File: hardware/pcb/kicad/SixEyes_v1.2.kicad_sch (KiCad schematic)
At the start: 49 parts, among them M1 NEMA17 40mm, U1 AS5600 Module

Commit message: Update the joint board for UART mode and the new pin map
MS1 and MS2 move to GPIO15 and GPIO16, UART TX to GPIO5, and the module's VREF
pad is read on GPIO2 through a new 10k resistor (R5). Adds the JDR4 socket for
the module's VREF and DIAG pads, VM and EN markers, a corrected regulator label,
JLCPCB 4-layer stackup and limits, net classes, and custom design rules for
power track widths, via sizes and the CAN pair. BOM gains the second 10k
resistor and JDR4.
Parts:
- added JDR4: Conn_01x02, Connector_PinSocket_2.54mm:PinSocket_1x02_P2.54mm_Vertical, symbol Connector_Generic:Conn_01x02
- added R5: MF1/4W-10KΩ±1% T52, SixEyes_v1.2:RES-TH_BD2.3-L6.5-P10.50-D0.5, symbol SixEyes_v1.2:MF1_4W-10KΩ±1%T52
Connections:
- net CANL is gone; now on net CAN+: JCN1.2, JCN2.2
- net CANL- is gone; now on net CAN-: JCN3.2 (Pin_2), UCN1.6 (CANL)
- net GND: no longer JDR1.2 (Pin_2), JDR1.3 (Pin_3)
- net UART_TX: now also JMC1.8 (Pin_8); no longer JMC1.5 (Pin_5)
- net MS2: now reaches JMC1.1 (Pin_1)
- net MS2: now also JDR1.3 (Pin_3)
- net 5V_PAD: now reaches D1.2 (K), JMC2.1 (Pin_1)
- net MS1: now reaches JMC2.7 (Pin_7)
- net MS1: now also JDR1.2 (Pin_2)
- net CANH renamed CAN-
- net CANH+ renamed CAN+
- new net DIAG: JDR4.2 (Pin_2)
- new net VREF_ADC: JMC1.5 (Pin_5), R5.2
- new net VREF_DR: JDR4.1 (Pin_1), R5.1
- no-connect marks 6 -> 4
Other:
- moved on the sheet: D1, JMC1, JMC2, R3

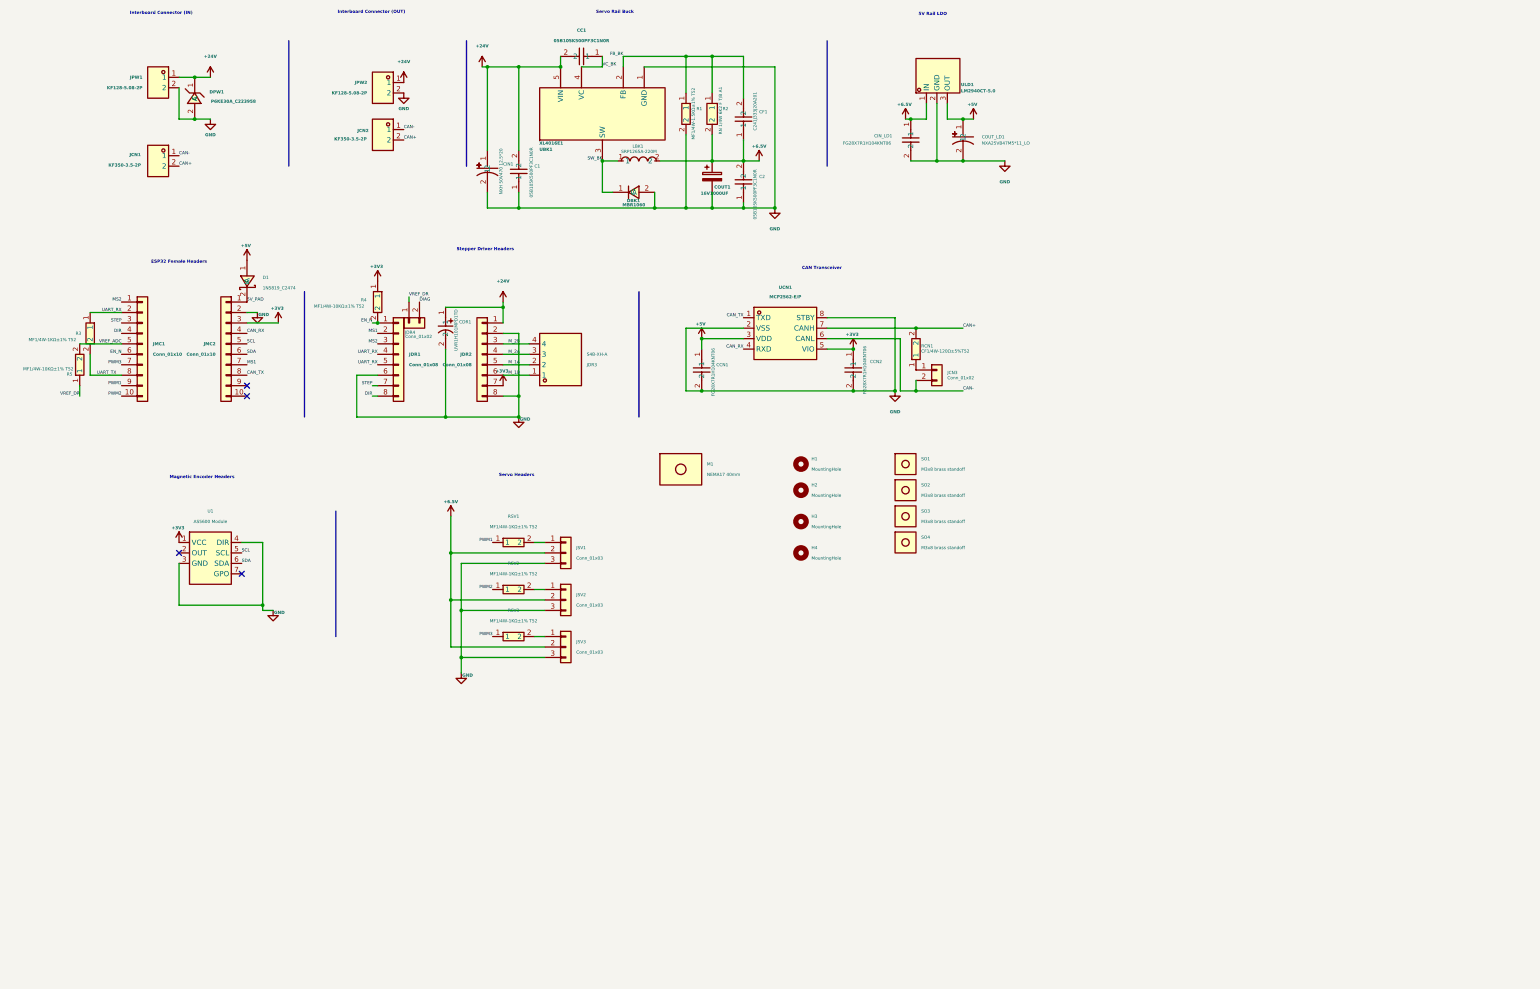
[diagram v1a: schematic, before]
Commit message: Release PCB v1.2: Studio Sanka title block, signed drawings, fabrication files
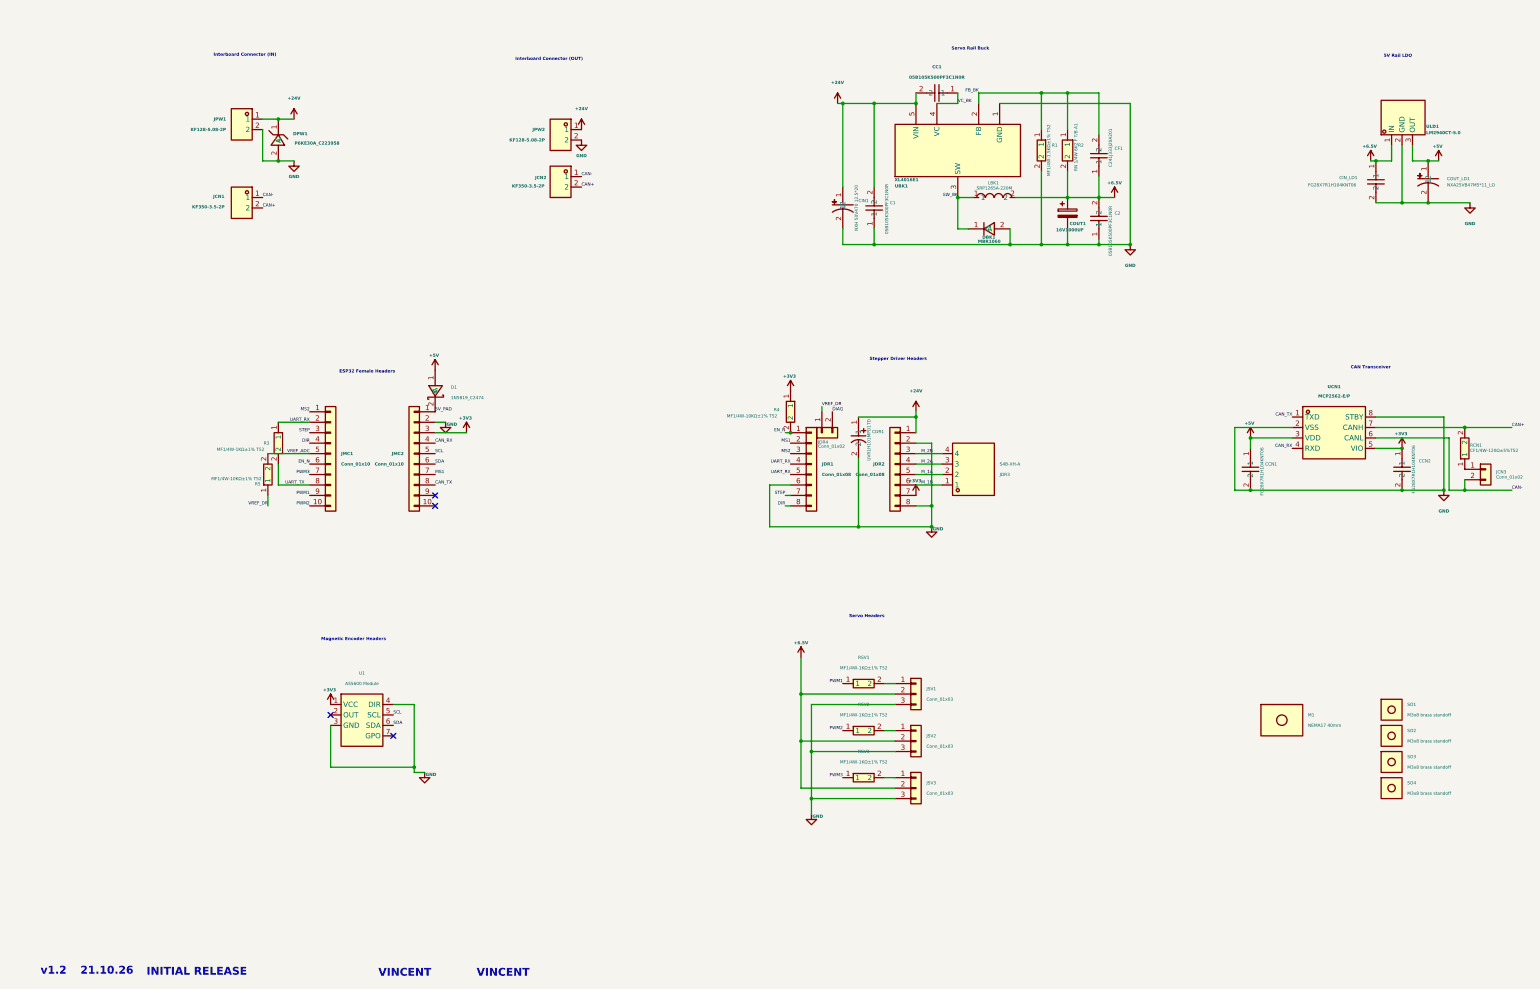
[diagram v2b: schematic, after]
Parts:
- removed H1, H2, H3, H4: MountingHole, MountingHole:MountingHole_3.2mm_M3, symbol Mechanical:MountingHole
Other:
- note added: "21.10.26"
- note added: "INITIAL RELEASE"
- note added: "VINCENT"
- note added: "v1.2"
- moved on the sheet: C1, C2, CC1, CCN1, CCN2, CDR1, CF1, CIN1, CIN_LD1, COUT1, COUT_LD1, D1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
